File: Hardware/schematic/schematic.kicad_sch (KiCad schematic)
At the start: 10 parts

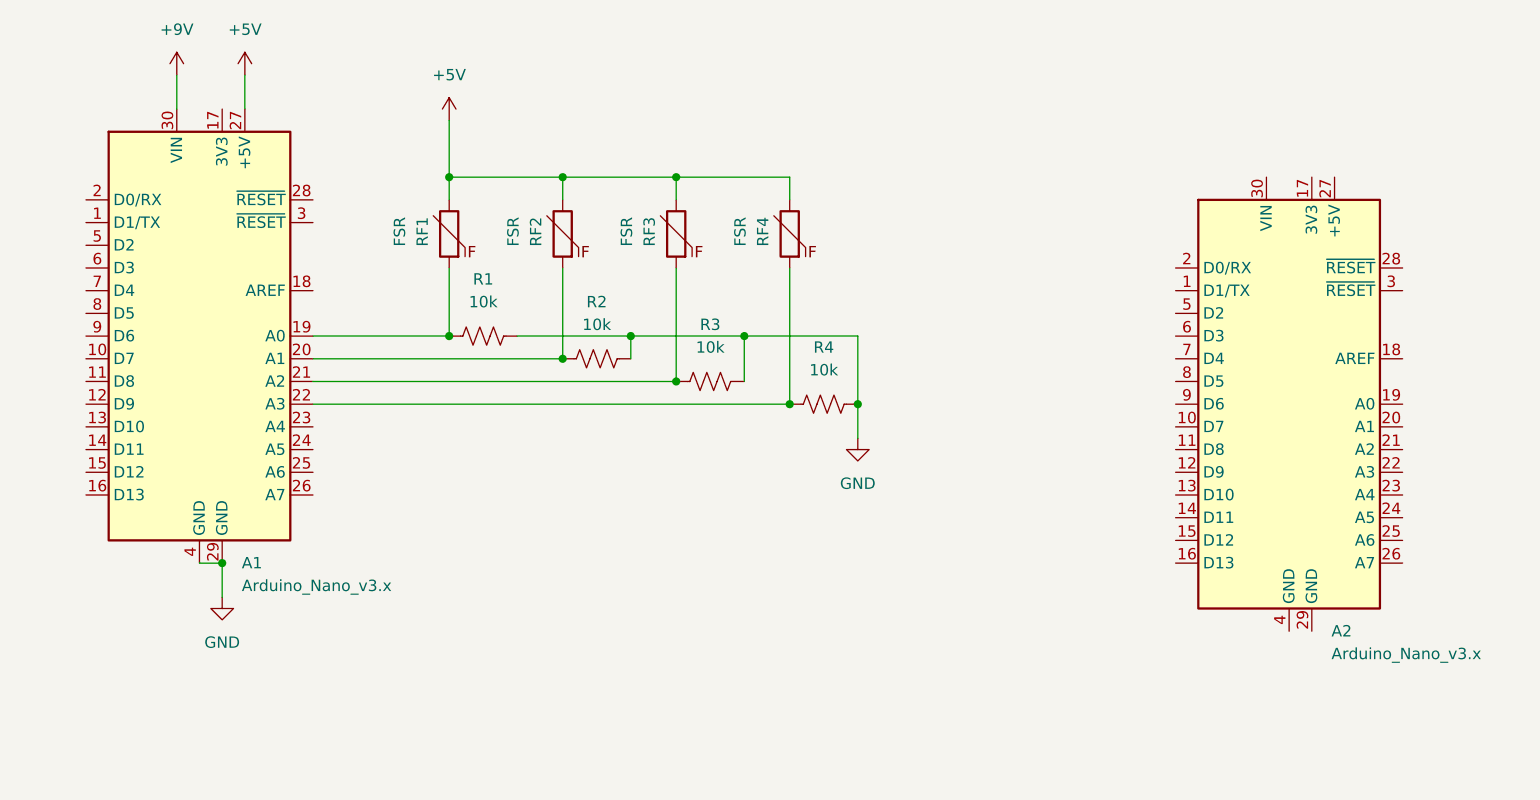
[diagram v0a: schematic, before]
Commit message: Complete fsr_bt_testing, start comm_testing
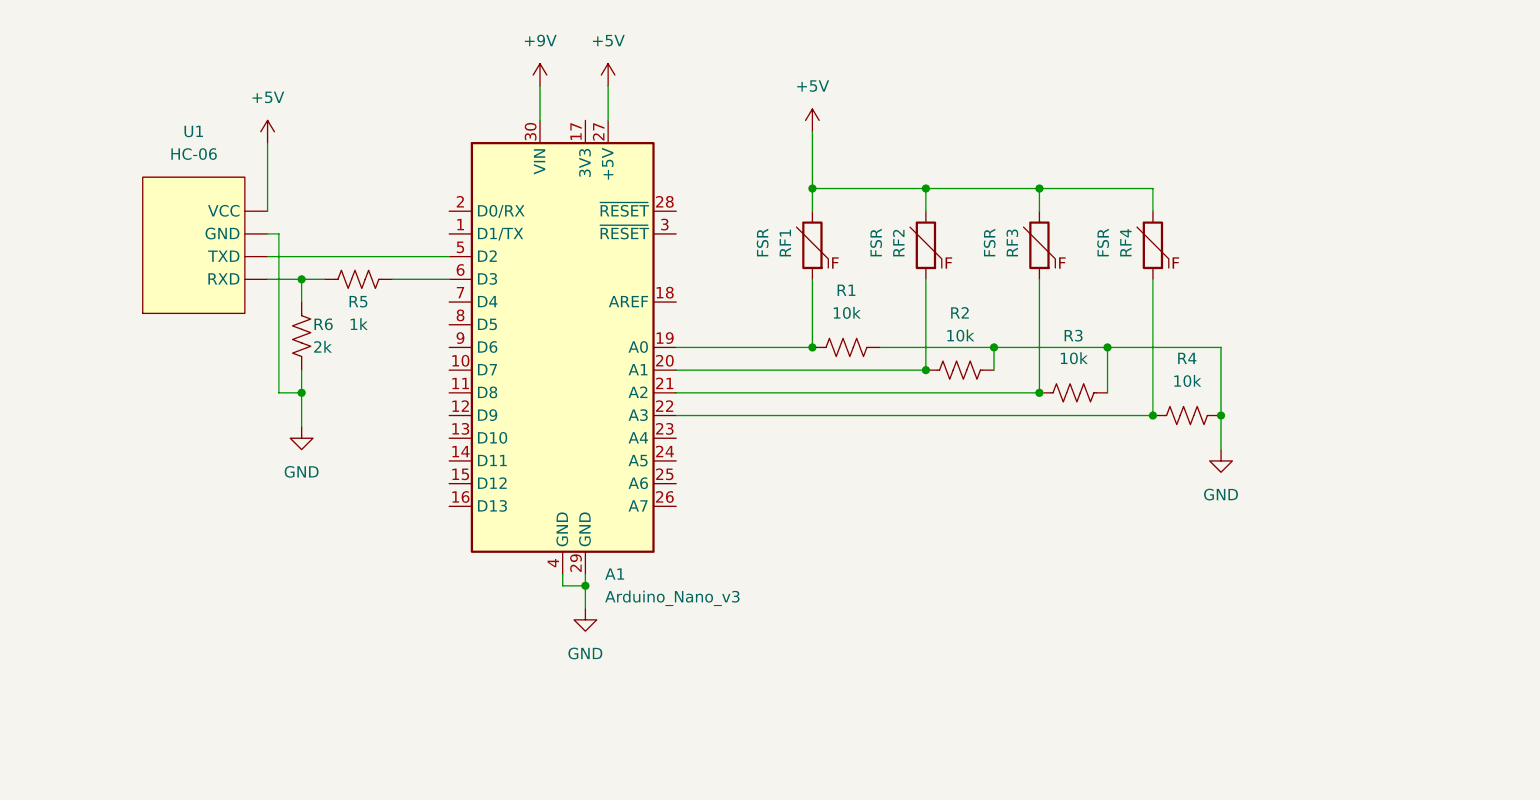
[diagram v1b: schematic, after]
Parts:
- removed A2: Arduino_Nano_v3.x, Module:Arduino_Nano, symbol MCU_Module:Arduino_Nano_v3.x
- added R5: 1k, symbol Device:R_US
- added R6: 2k, symbol Device:R_US
- added U1: HC-06, symbol extras:HC-06
- A1: value Arduino_Nano_v3.x -> Arduino_Nano_v3
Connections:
- net +5V: now also U1. (VCC)
- net GND: now also R6.2, U1. (VCC)
- net at A1.5 (D2): now also U1. (VCC)
- net at A1.6 (D3): now also R5.2
- new net: R5.1, R6.1, U1. (VCC)
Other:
- moved on the sheet: A1, R1, R2, R3, R4, RF1, RF2, RF3, RF4

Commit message: Update schematic, finalize nano firmware
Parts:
- added LS1: PS1240P02BT, PS1240P02BT:XDCR_PS1240P02BT, symbol Piezo_Speaker:PS1240P02BT
- added P1: SEN-11574, SEN-11574:XDCR_SEN-11574, symbol PulseSensor:SEN-11574
- added R7: 100, symbol Device:R_US
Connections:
- net GND: now also LS1.2, P1.3 (GND)
- net +3.3V: now reaches A1.17 (3V3)
- net +3.3V: now also P1.2 (V+)
- net at A1.23 (A4): now also P1.1 (SIGNAL)
- net at A1.7 (D4): now also R7.1
- new net: LS1.1, R7.2
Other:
- note added: "Bluetooth Module"
- note added: "Force-sensing Resistors"
- note added: "Pulse Sensor"
- note added: "Warning Buzzer"
- moved on the sheet: A1, R1, R2, R3, R4, R5, R6, RF1, RF2, RF3, RF4, U1
